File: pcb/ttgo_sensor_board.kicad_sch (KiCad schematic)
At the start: 59 parts, among them J1 Conn_01x13_Female, J2 Conn_01x13_Female, J3 Conn_01x03_Female, J4 Conn_01x03_Female, J5 Conn_01x04_Female, J6 Conn_01x04_Female, J7 Conn_01x04_Female, Q1 Q_NMOS_GSD, Q2 Q_NMOS_GSD, U1 BME680, U2 TCA9800, U3 TLV70218_SOT23-5, U4 LSM6DS3, U5 VEML7700

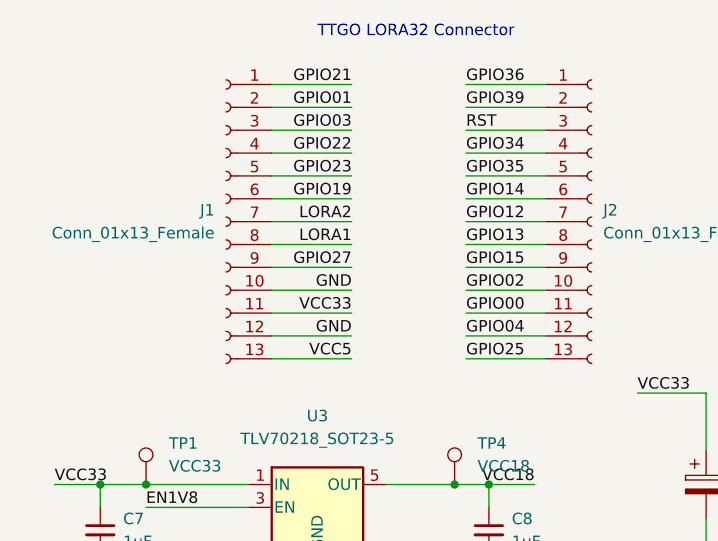
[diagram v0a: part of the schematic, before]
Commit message: fix gpio 26
gpio 26 was wrongly labeled as gpio 25 in schematic
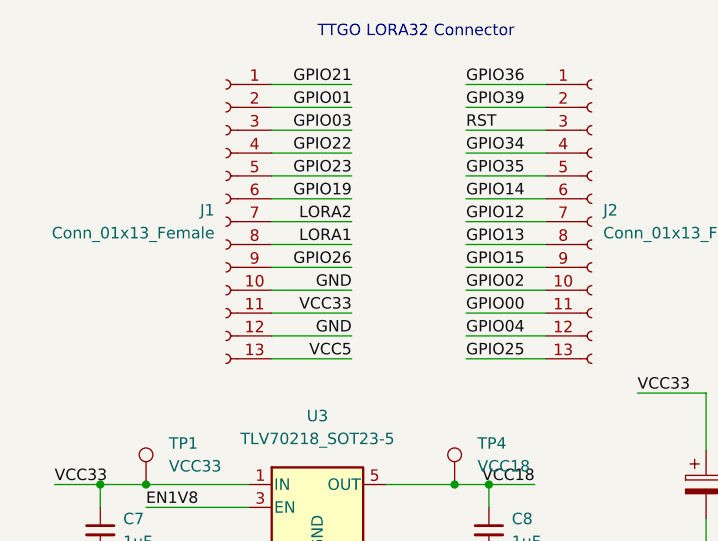
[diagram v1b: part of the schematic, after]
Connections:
- net GPIO27 renamed GPIO26
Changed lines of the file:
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@@
     (effects (font (size 1.27 1.27)) (justify left bottom))
   )
-  (label "GPIO27" (at 50.8 44.45 180)
+  (label "GPIO26" (at 50.8 44.45 180)
     (effects (font (size 1.27 1.27)) (justify right bottom))
   )

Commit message: changes to schematic
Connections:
- net GPIO13 is gone; now on net 1WIRE_DATA0: J2.8 (Pin_8)
- net 1WIRE_DATA0: no longer J2.10 (Pin_10)
- net GPIO00 renamed BOOT_0
- new net BOOT_1: J2.10 (Pin_10)
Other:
- note added: "LORA module: GPIO27 MOSI GPIO05 SCLK GPIO28 CS GPIO26 DIO GPIO23 RST GPIO19 MISO"
- note added: "OLED GPIO21 SDA GPIO22 SCL"
- note added: "TF CARD GPIO13 CS GPIO15 MOSI GPIO14 SCK GPIO02 MISO"
- moved on the sheet: C11, C12, C3, C4, C5, C6, J1, J2, R3, R4, R5, R6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
